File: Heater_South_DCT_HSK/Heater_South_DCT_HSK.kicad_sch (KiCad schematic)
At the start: 3 parts, among them J1 SHB1, J2 SHB2, J3 Heater South

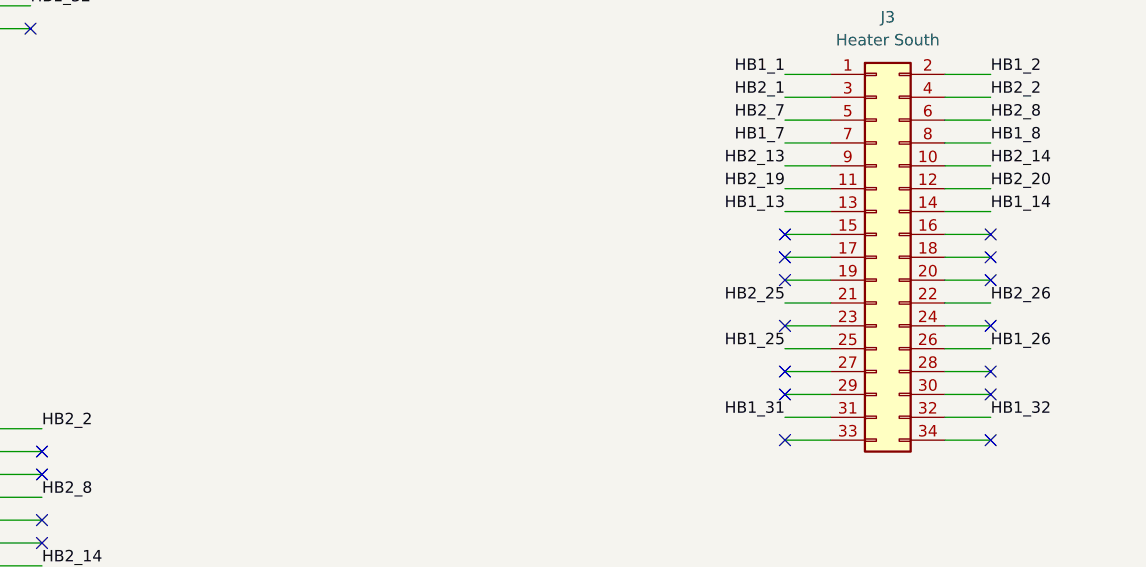
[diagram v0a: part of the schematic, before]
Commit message: New feedthrough PCBs to access spare heater channels for flowcontroller heaters.
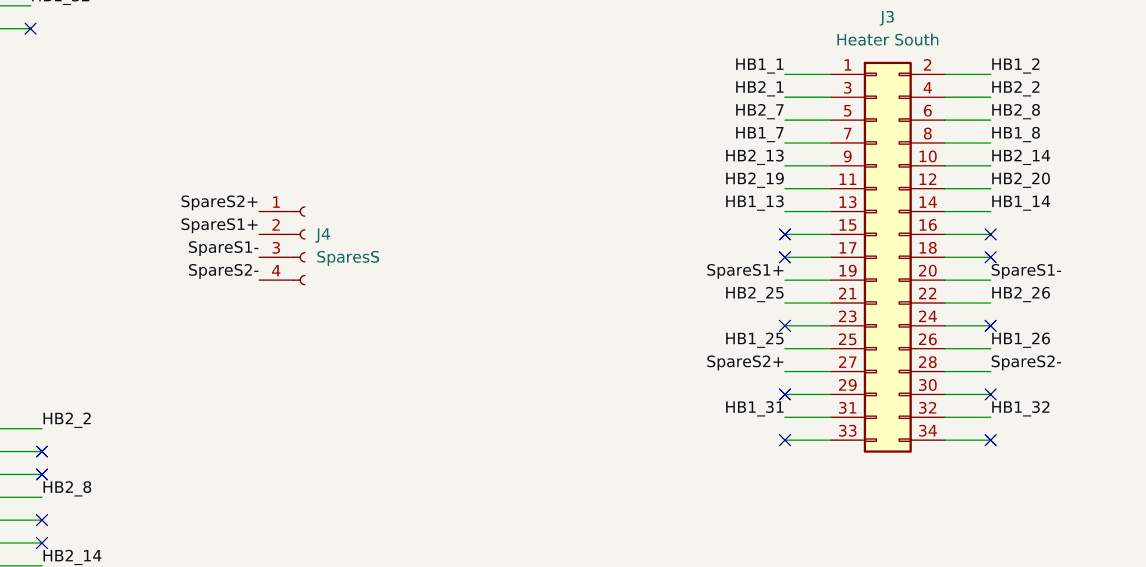
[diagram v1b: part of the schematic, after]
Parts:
- added J4: SparesS, Connector_Molex:Molex_Micro-Fit_3.0_43045-0400_2x02_P3.00mm_Horizontal, symbol Connector:Conn_01x04_Socket
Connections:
- net SpareS1+: now reaches J3.19 (Pin_19)
- net SpareS1+: now also J4.2 (Pin_2)
- net SpareS1-: now reaches J3.20 (Pin_20)
- net SpareS1-: now also J4.3 (Pin_3)
- net SpareS2+: now reaches J3.27 (Pin_27)
- net SpareS2+: now also J4.1 (Pin_1)
- net SpareS2-: now reaches J3.28 (Pin_28)
- net SpareS2-: now also J4.4 (Pin_4)
- no-connect marks 62 -> 58
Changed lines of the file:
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@@
   (no_connect (at 101.6 74.93))
   (no_connect (at 78.74 82.55))
-  (no_connect (at 208.28 120.65))
   (no_connect (at 185.42 123.19))
   (no_connect (at 78.74 62.23))
   (no_connect (at 101.6 82.55))
   (no_connect (at 185.42 107.95))
-  (no_connect (at 208.28 110.49))
   (no_connect (at 208.28 123.19))
   (no_connect (at 101.6 62.23))
-  (no_connect (at 185.42 110.49))
   (no_connect (at 101.6 59.69))
   (no_connect (at 102.87 167.64))
@@
   (no_connect (at 208.28 105.41))
   (no_connect (at 101.6 67.31))
-  (no_connect (at 185.42 120.65))
   (no_connect (at 78.74 59.69))
   (no_connect (at 101.6 69.85))
@@
     (effects (font (size 1.27 1.27)) (justify right bottom))
   )
+  (label "SpareS2-" (at 127 110.49 180) (fields_autoplaced)
+    (effects (font (size 1.27 1.27)) (justify right bottom))
+  )
   (label "HB1_32" (at 101.6 80.01 0) (fields_autoplaced)
     (effects (font (size 1.27 1.27)) (justify left bottom))
@@
     (effects (font (size 1.27 1.27)) (justify right bottom))
   )
+  (label "SpareS1+" (at 185.42 110.49 180) (fields_autoplaced)
+    (effects (font (size 1.27 1.27)) (justify right bottom))
+  )
   (label "HB2_20" (at 208.28 100.33 0) (fields_autoplaced)
     (effects (font (size 1.27 1.27)) (justify left bottom))
@@
     (effects (font (size 1.27 1.27)) (justify left bottom))
   )
+  (label "SpareS1+" (at 127 105.41 180) (fields_autoplaced)
+    (effects (font (size 1.27 1.27)) (justify right bottom))
+  )
+  (label "SpareS2+" (at 185.42 120.65 180) (fields_autoplaced)
+    (effects (font (size 1.27 1.27)) (justify right bottom))
+  )
   (label "HB1_31" (at 78.74 80.01 180) (fields_autoplaced)
     (effects (font (size 1.27 1.27)) (justify right bottom))
@@
     (effects (font (size 1.27 1.27)) (justify right bottom))
   )
+  (label "SpareS2-" (at 208.28 120.65 0) (fields_autoplaced)
+    (effects (font (size 1.27 1.27)) (justify left bottom))
+  )
+  (label "SpareS2+" (at 127 102.87 180) (fields_autoplaced)
+    (effects (font (size 1.27 1.27)) (justify right bottom))
+  )
   (label "HB1_2" (at 101.6 41.91 0) (fields_autoplaced)
     (effects (font (size 1.27 1.27)) (justify left bottom))
@@
     (effects (font (size 1.27 1.27)) (justify right bottom))
   )
+  (label "SpareS1-" (at 208.28 110.49 0) (fields_autoplaced)
+    (effects (font (size 1.27 1.27)) (justify left bottom))
+  )
   (label "HB2_8" (at 102.87 134.62 0) (fields_autoplaced)
     (effects (font (size 1.27 1.27)) (justify left bottom))
@@
     (effects (font (size 1.27 1.27)) (justify left bottom))
   )
+  (label "SpareS1-" (at 127 107.95 180) (fields_autoplaced)
+    (effects (font (size 1.27 1.27)) (justify right bottom))
+  )
   (label "HB2_8" (at 208.28 92.71 0) (fields_autoplaced)
     (effects (font (size 1.27 1.27)) (justify left bottom))
+  )
+  (symbol (lib_id "Connector:Conn_01x04_Socket") (at 132.08 105.41 0) (unit 1)
+    (in_bom yes) (on_board yes) (dnp no) (fields_autoplaced)
+    (property "Reference" "J4" (at 133.35 105.41 0)
+      (effects (font (size 1.27 1.27)) (justify left))
+    )
+    (property "Value" "SparesS" (at 133.35 107.95 0)
+      (effects (font (size 1.27 1.27)) (justify left))
+    )
+    (property "Footprint" "Connector_Molex:Molex_Micro-Fit_3.0_43045-0400_2x02_P3.00mm_Horizontal" (at 132.08 105.41 0)
+      (effects (font (size 1.27 1.27)) hide)
+    )
+    (property "Datasheet" "~" (at 132.08 105.41 0)
+      (effects (font (size 1.27 1.27)) hide)
+    )
+    (pin "1")
+    (pin "2")
+    (pin "3")
+    (pin "4")
+    (instances
+      (project "Heater_South_DCT_HSK"
+        (path "/b67bdb50-32e2-49f2-b2ed-35caa82406e6"
+          (reference "J4") (unit 1)
+        )
+      )
+    )
   )
   (symbol (lib_id "Connector_Generic:Conn_02x17_Odd_Even") (at 195.58 107.95 0) (unit 1)
@@
     (pin "9")
     (instances
-      (project "Heater_North_DCT_HSK"
+      (project "Heater_South_DCT_HSK"
         (path "/b67bdb50-32e2-49f2-b2ed-35caa82406e6"
           (reference "J3") (unit 1)
@@
     (pin "9")
     (instances
-      (project "Heater_North_DCT_HSK"
+      (project "Heater_South_DCT_HSK"
         (path "/b67bdb50-32e2-49f2-b2ed-35caa82406e6"
           (reference "J1") (unit 1)
@@
     (pin "9")
     (instances
-      (project "Heater_North_DCT_HSK"
+      (project "Heater_South_DCT_HSK"
         (path "/b67bdb50-32e2-49f2-b2ed-35caa82406e6"
           (reference "J2") (unit 1)
